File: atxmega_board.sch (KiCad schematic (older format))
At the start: 23 parts, among them CON1 BUQ2-USB-MINI-B, IC1 BUQ2-ATXMEGA128A4U-A, SW1 SW_PUSH

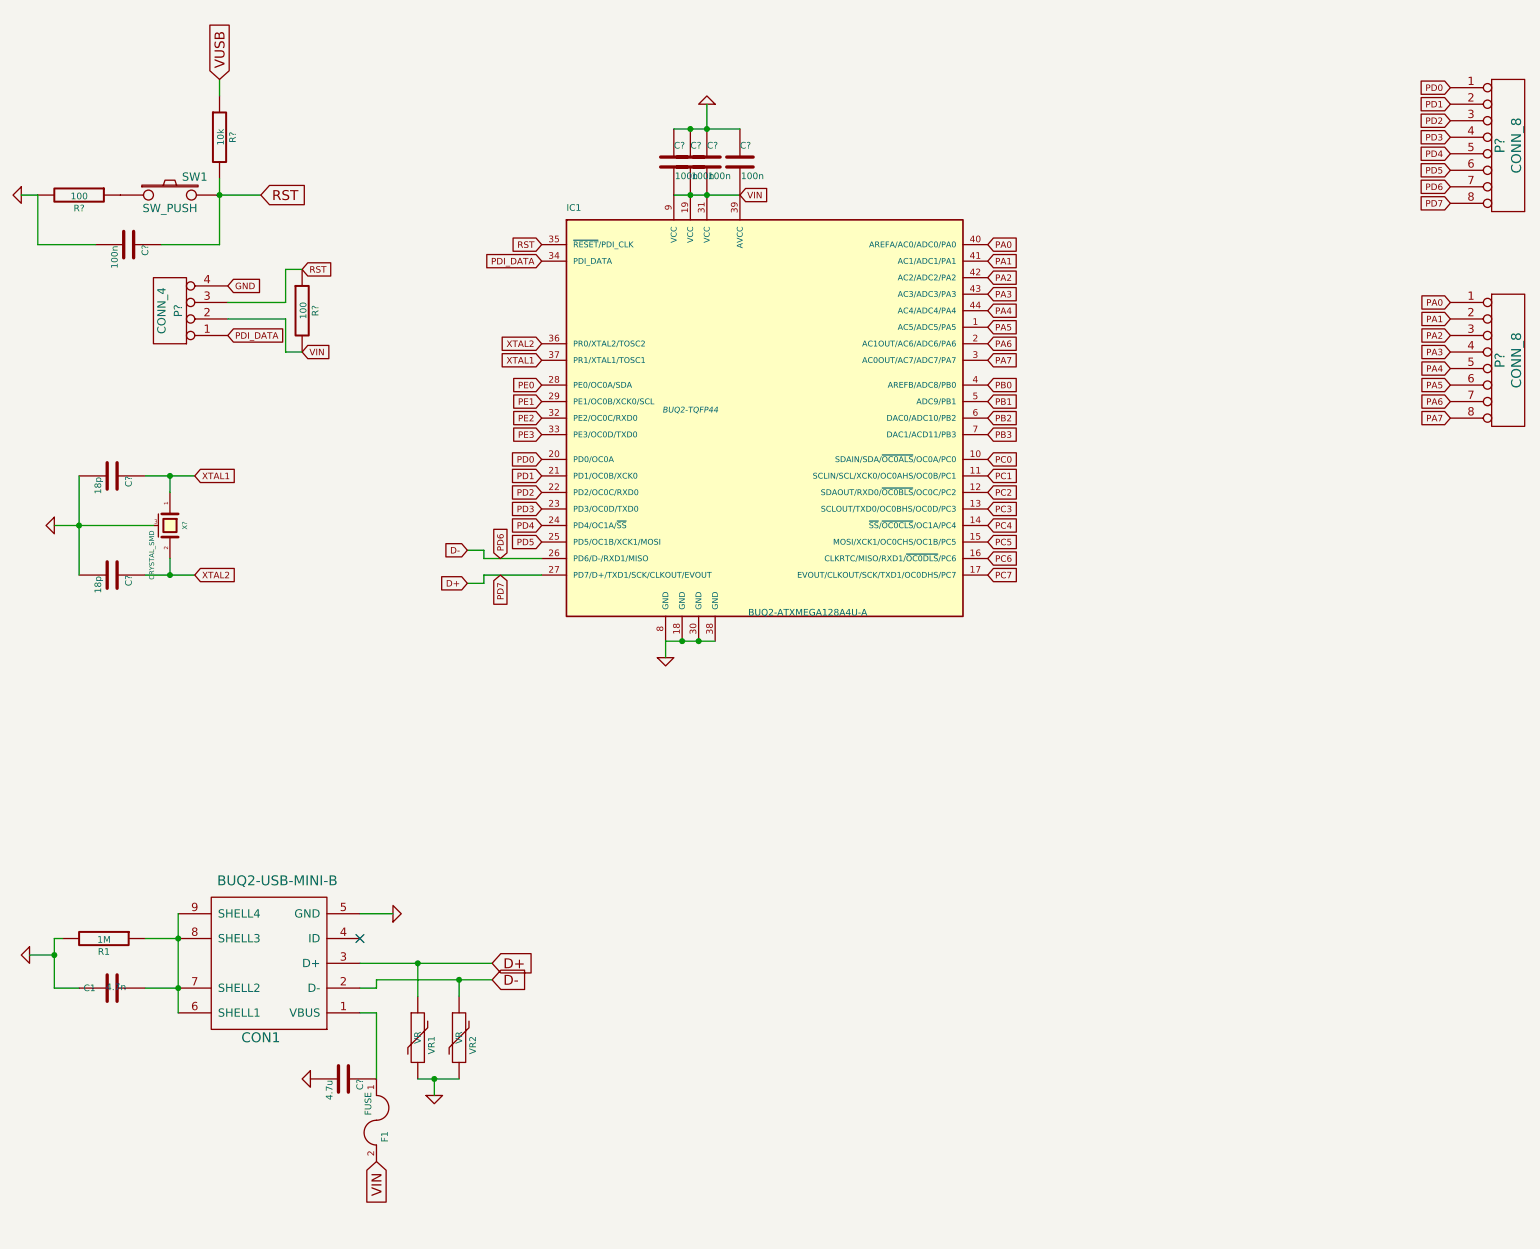
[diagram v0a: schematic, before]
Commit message: Round edges
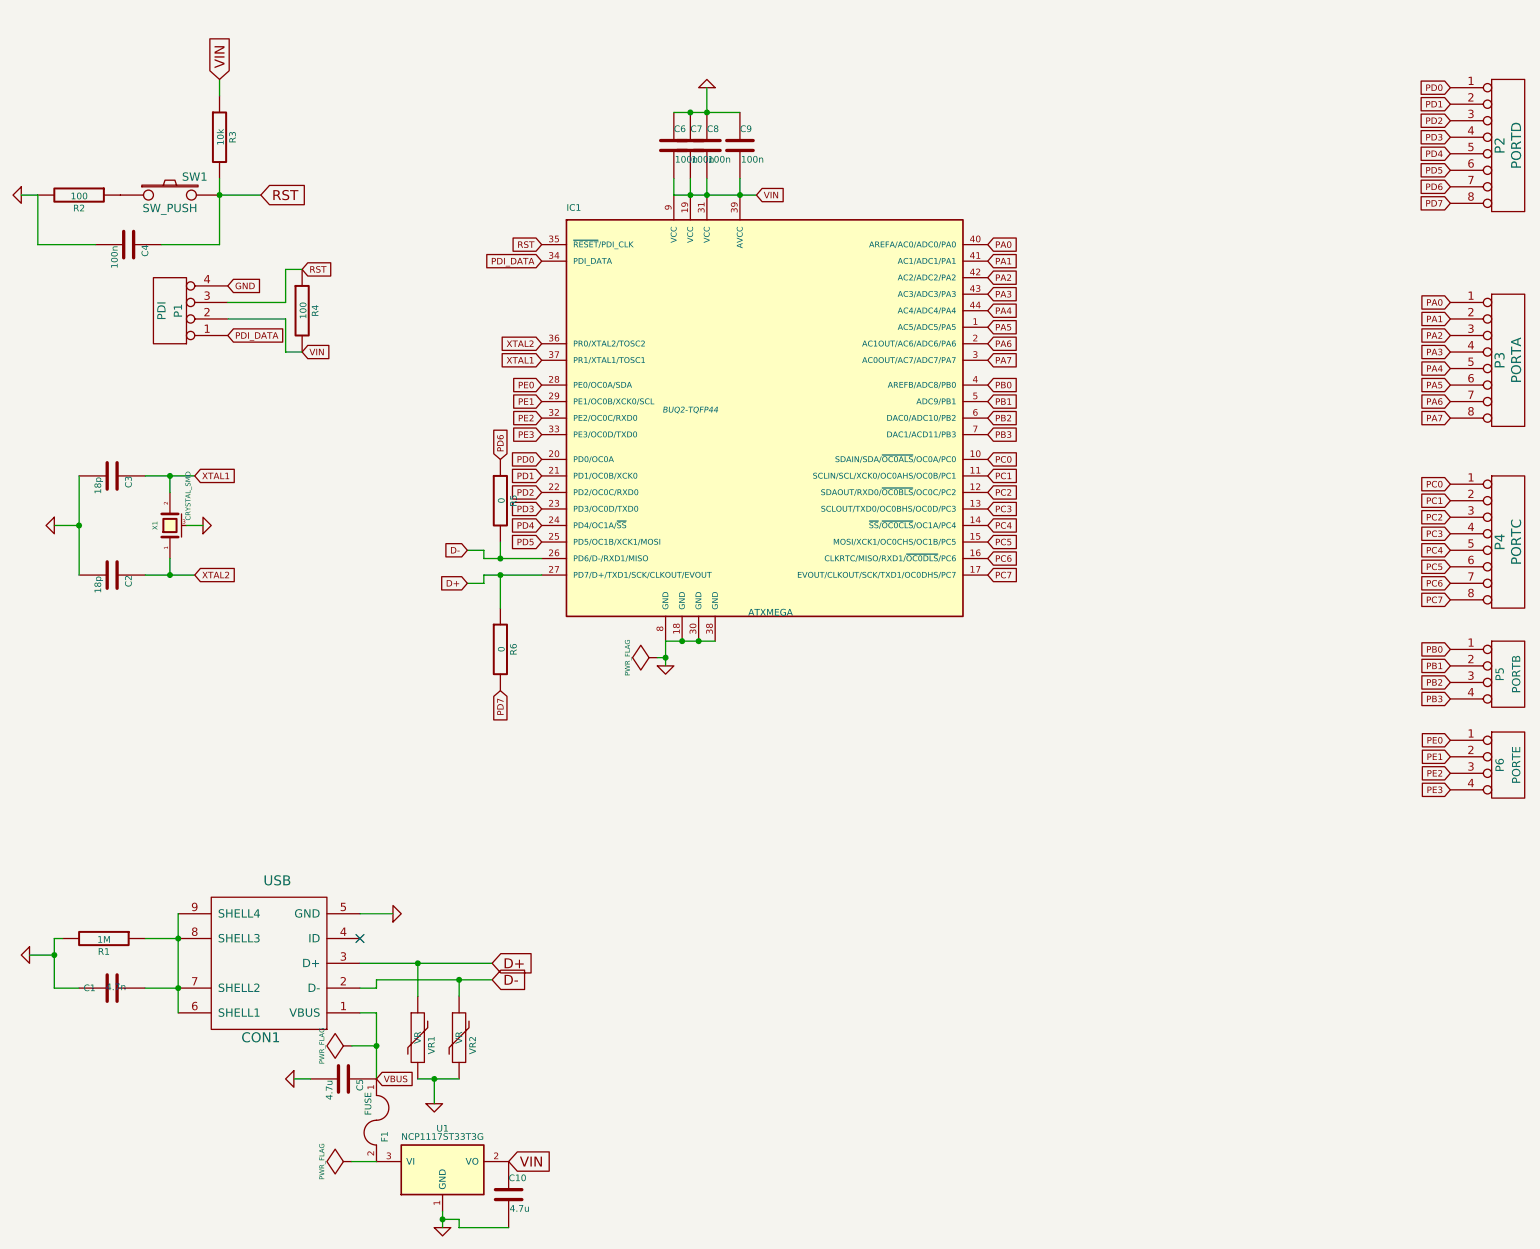
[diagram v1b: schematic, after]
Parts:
- added C10: 4.7u, SM0805, symbol C
- added P4: PORTC, symbol CONN_8
- added P5: PORTB, symbol CONN_4
- added P6: PORTE, symbol CONN_4
- added R5, R6: 0, SM0603, symbol R
- added U1: NCP1117ST33T3G, symbol NCP1117ST33T3G
- CON1: value BUQ2-USB-MINI-B -> USB
- IC1: value BUQ2-ATXMEGA128A4U-A -> ATXMEGA
- P1: renamed from P?; value CONN_4 -> PDI
- P2: renamed from P?; value CONN_8 -> PORTD
- P3: renamed from P?; value CONN_8 -> PORTA
- X1: renamed from X?; footprint (none) -> SM_CRYSTAL_4_LEAD
- gave numbers to parts that had none: 11
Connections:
- net VUSB is gone; now on net VIN: R3.1
- net D+: now also R6.1; no longer P2.8 (P8)
- net D-: now also R5.2; no longer P2.7 (P7)
- net GND: now also C10.2, U1.1 (GND)
- net PB0: now also P5.1 (P1)
- net PB1: now also P5.2 (P2)
- net PB2: now also P5.3 (P3)
- net PB3: now also P5.4 (P4)
- net PC0: now also P4.1 (P1)
- net PC1: now also P4.2 (P2)
- net PC2: now also P4.3 (P3)
- net PC3: now also P4.4 (P4)
- net PC4: now also P4.5 (P5)
- net PC5: now also P4.6 (P6)
- net PC6: now also P4.7 (P7)
- net PC7: now also P4.8 (P8)
- net PE0: now also P6.1 (P1)
- net PE1: now also P6.2 (P2)
- net PE2: now also P6.3 (P3)
- net PE3: now also P6.4 (P4)
- net VIN: now also C10.1, U1.2 (VO); no longer F1.2
- net XTAL1: now also C3.1, X1.2; no longer C2.1, X1.1
- net XTAL2: now also C2.1, X1.1; no longer C3.1, X1.2
- net VBUS: now reaches C5.1, CON1.1 (VBUS), F1.1
- new net: F1.2, U1.3 (VI)
- new net PD6: P2.7 (P7), R5.1
- new net PD7: P2.8 (P8), R6.2
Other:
- moved on the sheet: C2, C3, C6, C7, C8, C9, X1

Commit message: Update parts
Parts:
- F1: Digikey (none) -> MF-MSMF050-2CT-ND
- IC1: Digikey (none) -> ATXMEGA128A4U-AU-ND
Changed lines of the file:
@@
 F 1 "ATXMEGA" H 4950 1750 40  0000 L BNN
 F 2 "BUQ2-TQFP44" H 4600 3000 35  0000 C CIN
-F 3 "~" H 4600 3000 60  0000 C CNN
+F 3 "http://www.atmel.com/Images/Atmel-8387-8-and16-bit-AVR-Microcontroller-XMEGA-A4U_Datasheet.pdf" H 4600 3000 60  0001 C CNN
+F 4 "ATXMEGA128A4U-AU-ND" H 4600 3000 60  0001 C CNN "Digikey"
 	1    4600 3000
 	1    0    0    -1
@@
 F 1 "FUSE" H 2600 7250 40  0000 C CNN
 F 2 "" H 2700 7300 60  0000 C CNN
-F 3 "" H 2700 7300 60  0000 C CNN
+F 3 "http://www.bourns.com/data/global/pdfs/mfmsmf.pdf" H 2700 7300 60  0001 C CNN
+F 4 "MF-MSMF050-2CT-ND" H 2700 7300 60  0001 C CNN "Digikey"
 	1    2700 7300
 	0    1    1    0
@@
 F 1 "SW_PUSH" H 1450 1620 50  0000 C CNN
 F 2 "PUSHBUTTON_4x4" H 1450 1700 60  0001 C CNN
-F 3 "" H 1450 1700 60  0000 C CNN
+F 3 "http://www.apem.com/files/apem/brochures/MJTP_6MM_4MM_SMD.pdf" H 1450 1700 60  0001 C CNN
 F 4 "679-2420-2-ND (ebaysta)" H 1450 1700 60  0001 C CNN "Digikey"
 	1    1450 1700
@@
 F 0 "#PWR013" H 3100 7950 30  0001 C CNN
 F 1 "GND" H 3100 7880 30  0001 C CNN
-F 2 "" H 3100 7950 0   0000 C CNN
-F 3 "" H 3100 7950 0   0000 C CNN
+F 2 "" H 3100 7950 60  0000 C CNN
+F 3 "" H 3100 7950 60  0000 C CNN
 	1    3100 7950
 	1    0    0    -1
